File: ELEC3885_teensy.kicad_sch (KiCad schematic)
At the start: 0 parts

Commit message: Schematic work
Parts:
- added J6, J7: Conn_01x24_Female, Connector_PinSocket_2.54mm:PinSocket_1x24_P2.54mm_Vertical, symbol Connector:Conn_01x24_Female
- added U3: Teensy4.1, teensy:Teensy41, symbol teensy:Teensy4.1
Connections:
- new net: J7.1 (Pin_1), U3.48 (VIN)
- new net: J7.10 (Pin_10), U3.39 (17_A3_TX4_SDA1)
- new net: J7.11 (Pin_11), U3.38 (16_A2_RX4_SCL1)
- new net: J7.13 (Pin_13), U3.36 (14_A0_TX3_SPDIF_OUT)
- new net: J7.14 (Pin_14), U3.35 (13_SCK_LED)
- new net: J7.16 (Pin_16), U3.33 (41_A17)
- new net: J7.17 (Pin_17), U3.32 (40_A16)
- new net: J7.18 (Pin_18), U3.31 (39_MISO1_OUT1A)
- new net: J7.19 (Pin_19), U3.30 (38_CS1_IN1)
- new net: J7.20 (Pin_20), U3.29 (37_CS)
- new net: J7.21 (Pin_21), U3.28 (36_CS)
- new net: J7.22 (Pin_22), U3.27 (35_TX8)
- new net: J7.23 (Pin_23), U3.26 (34_RX8)
- new net: J7.24 (Pin_24), U3.25 (33_MCLK2)
- new net: J7.5 (Pin_5), U3.44 (22_A8_CTX1)
- new net: J6.1 (Pin_1), U3.24 (32_OUT1B)
- new net: J6.11 (Pin_11), U3.14 (12_MISO_MQSL)
- new net: J6.12 (Pin_12), U3.13 (11_MOSI_CTX1)
- new net: J6.13 (Pin_13), U3.12 (10_CS_MQSR)
- new net: J6.14 (Pin_14), U3.11 (9_OUT1C)
- new net: J6.17 (Pin_17), U3.8 (6_OUT1D)
- new net: J6.18 (Pin_18), U3.7 (5_IN2)
- new net: J6.19 (Pin_19), U3.6 (4_BCLK2)
- new net: J6.2 (Pin_2), U3.23 (31_CTX3)
- new net: J6.20 (Pin_20), U3.5 (3_LRCLK2)
- new net: J6.21 (Pin_21), U3.4 (2_OUT2)
- new net: J6.22 (Pin_22), U3.3 (1_TX1_CTX2_MISO1)
- new net: J6.23 (Pin_23), U3.2 (0_RX1_CRX2_CS1)
- new net: J6.3 (Pin_3), U3.22 (30_CRX3)
- new net: J6.4 (Pin_4), U3.21 (29_TX7)
- new net: J6.5 (Pin_5), U3.20 (28_RX7)
- new net: J6.6 (Pin_6), U3.19 (27_A13_SCK1)
- new net: J6.7 (Pin_7), U3.18 (26_A12_MOSI1)
- new net: J6.8 (Pin_8), U3.17 (25_A11_RX6_SDA2)
- new net: J6.9 (Pin_9), U3.16 (24_A10_TX6_SCL2)
- new net +3.3V: J6.10 (Pin_10), J7.3 (Pin_3), U3.15 (3V3), U3.46 (3V3)
- new net BCLK: J7.6 (Pin_6), U3.43 (21_A7_RX5_BCLK1)
- new net D_IN: J6.15 (Pin_15), U3.10 (8_TX2_IN1)
- new net D_OUT: J6.16 (Pin_16), U3.9 (7_RX2_OUT1A)
- new net GND: J6.24 (Pin_24), J7.15 (Pin_15), J7.2 (Pin_2), U3.1 (GND), U3.34 (GND), U3.47 (GND)
- new net LRCLK: J7.7 (Pin_7), U3.42 (20_A6_TX5_LRCLK1)
- new net MCLK: J7.4 (Pin_4), U3.45 (23_A9_CRX1_MCLK1)
- new net SCL: J7.8 (Pin_8), U3.41 (19_A5_SCL)
- new net SDA: J7.9 (Pin_9), U3.40 (18_A4_SDA)
- new net VOLUME_CONTROL: J7.12 (Pin_12), U3.37 (15_A1_RX3_SPDIF_IN)

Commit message: Initial schematic complete
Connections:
- net BUTTON_0: now reaches J7.21 (Pin_21), U3.28 (36_CS)
- net BUTTON_1: now reaches J7.22 (Pin_22), U3.27 (35_TX8)
- net BUTTON_2: now reaches J7.23 (Pin_23), U3.26 (34_RX8)
- net BUTTON_3: now reaches J7.24 (Pin_24), U3.25 (33_MCLK2)
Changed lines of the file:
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@@
 (kicad_sch (version 20211123) (generator eeschema)
   (paper "A4")
+  (junction (at 151.13 104.14) (diameter 0) (color 0 0 0 0)
+  )
   (junction (at 80.01 71.12) (diameter 0) (color 0 0 0 0)
   )
@@
   (junction (at 151.13 78.74) (diameter 0) (color 0 0 0 0)
   )
+  (junction (at 151.13 106.68) (diameter 0) (color 0 0 0 0)
+  )
+  (junction (at 151.13 109.22) (diameter 0) (color 0 0 0 0)
+  )
   (junction (at 151.13 63.5) (diameter 0) (color 0 0 0 0)
   )
   (junction (at 151.13 53.34) (diameter 0) (color 0 0 0 0)
   )
+  (junction (at 151.13 101.6) (diameter 0) (color 0 0 0 0)
+  )
   (junction (at 151.13 86.36) (diameter 0) (color 0 0 0 0)
   )
@@
     (stroke (width 0) (type default) (color 0 0 0 0))
   )
+  (wire (pts (xy 163.83 106.68) (xy 151.13 106.68))
+    (stroke (width 0) (type default) (color 0 0 0 0))
+  )
+  (wire (pts (xy 151.13 99.06) (xy 143.51 99.06))
+    (stroke (width 0) (type default) (color 0 0 0 0))
+  )
+  (wire (pts (xy 80.01 58.42) (xy 87.63 58.42))
+    (stroke (width 0) (type default) (color 0 0 0 0))
+  )
+  (wire (pts (xy 80.01 83.82) (xy 87.63 83.82))
+    (stroke (width 0) (type default) (color 0 0 0 0))
+  )
+  (wire (pts (xy 151.13 101.6) (xy 143.51 101.6))
+    (stroke (width 0) (type default) (color 0 0 0 0))
+  )
+  (wire (pts (xy 151.13 96.52) (xy 143.51 96.52))
+    (stroke (width 0) (type default) (color 0 0 0 0))
+  )
+  (wire (pts (xy 80.01 109.22) (xy 87.63 109.22))
+    (stroke (width 0) (type default) (color 0 0 0 0))
+  )
+  (wire (pts (xy 163.83 101.6) (xy 151.13 101.6))
+    (stroke (width 0) (type default) (color 0 0 0 0))
+  )
+  (wire (pts (xy 80.01 78.74) (xy 87.63 78.74))
+    (stroke (width 0) (type default) (color 0 0 0 0))
+  )
+  (wire (pts (xy 151.13 106.68) (xy 143.51 106.68))
+    (stroke (width 0) (type default) (color 0 0 0 0))
+  )
+  (wire (pts (xy 151.13 73.66) (xy 143.51 73.66))
+    (stroke (width 0) (type default) (color 0 0 0 0))
+  )
+  (wire (pts (xy 151.13 76.2) (xy 143.51 76.2))
+    (stroke (width 0) (type default) (color 0 0 0 0))
+  )
+  (wire (pts (xy 162.56 66.04) (xy 151.13 66.04))
+    (stroke (width 0) (type default) (color 0 0 0 0))
+  )
+  (wire (pts (xy 163.83 78.74) (xy 151.13 78.74))
+    (stroke (width 0) (type default) (color 0 0 0 0))
+  )
+  (wire (pts (xy 162.56 53.34) (xy 151.13 53.34))
+    (stroke (width 0) (type default) (color 0 0 0 0))
+  )
+  (wire (pts (xy 163.83 104.14) (xy 151.13 104.14))
+    (stroke (width 0) (type default) (color 0 0 0 0))
+  )
+  (wire (pts (xy 151.13 60.96) (xy 143.51 60.96))
+    (stroke (width 0) (type default) (color 0 0 0 0))
+  )
+  (wire (pts (xy 151.13 53.34) (xy 143.51 53.34))
+    (stroke (width 0) (type default) (color 0 0 0 0))
+  )
+  (wire (pts (xy 80.01 53.34) (xy 87.63 53.34))
+    (stroke (width 0) (type default) (color 0 0 0 0))
+  )
+  (wire (pts (xy 151.13 104.14) (xy 143.51 104.14))
+    (stroke (width 0) (type default) (color 0 0 0 0))
+  )
+  (wire (pts (xy 162.56 55.88) (xy 151.13 55.88))
+    (stroke (width 0) (type default) (color 0 0 0 0))
+  )
   (wire (pts (xy 151.13 109.22) (xy 143.51 109.22))
     (stroke (width 0) (type default) (color 0 0 0 0))
   )
-  (wire (pts (xy 151.13 99.06) (xy 143.51 99.06))
-    (stroke (width 0) (type default) (color 0 0 0 0))
-  )
-  (wire (pts (xy 80.01 58.42) (xy 87.63 58.42))
-    (stroke (width 0) (type default) (color 0 0 0 0))
-  )
-  (wire (pts (xy 80.01 83.82) (xy 87.63 83.82))
-    (stroke (width 0) (type default) (color 0 0 0 0))
-  )
-  (wire (pts (xy 151.13 96.52) (xy 143.51 96.52))
-    (stroke (width 0) (type default) (color 0 0 0 0))
-  )
-  (wire (pts (xy 80.01 109.22) (xy 87.63 109.22))
-    (stroke (width 0) (type default) (color 0 0 0 0))
-  )
-  (wire (pts (xy 80.01 78.74) (xy 87.63 78.74))
-    (stroke (width 0) (type default) (color 0 0 0 0))
-  )
-  (wire (pts (xy 151.13 73.66) (xy 143.51 73.66))
-    (stroke (width 0) (type default) (color 0 0 0 0))
-  )
-  (wire (pts (xy 151.13 76.2) (xy 143.51 76.2))
-    (stroke (width 0) (type default) (color 0 0 0 0))
-  )
-  (wire (pts (xy 162.56 66.04) (xy 151.13 66.04))
-    (stroke (width 0) (type default) (color 0 0 0 0))
-  )
-  (wire (pts (xy 163.83 78.74) (xy 151.13 78.74))
-    (stroke (width 0) (type default) (color 0 0 0 0))
-  )
-  (wire (pts (xy 162.56 53.34) (xy 151.13 53.34))
-    (stroke (width 0) (type default) (color 0 0 0 0))
-  )
-  (wire (pts (xy 151.13 106.68) (xy 143.51 106.68))
-    (stroke (width 0) (type default) (color 0 0 0 0))
-  )
-  (wire (pts (xy 151.13 60.96) (xy 143.51 60.96))
-    (stroke (width 0) (type default) (color 0 0 0 0))
-  )
-  (wire (pts (xy 151.13 53.34) (xy 143.51 53.34))
-    (stroke (width 0) (type default) (color 0 0 0 0))
-  )
-  (wire (pts (xy 80.01 53.34) (xy 87.63 53.34))
-    (stroke (width 0) (type default) (color 0 0 0 0))
-  )
-  (wire (pts (xy 162.56 55.88) (xy 151.13 55.88))
-    (stroke (width 0) (type default) (color 0 0 0 0))
-  )
   (wire (pts (xy 80.01 68.58) (xy 87.63 68.58))
     (stroke (width 0) (type default) (color 0 0 0 0))
@@
     (stroke (width 0) (type default) (color 0 0 0 0))
   )
-  (wire (pts (xy 151.13 104.14) (xy 143.51 104.14))
-    (stroke (width 0) (type default) (color 0 0 0 0))
-  )
   (wire (pts (xy 151.13 93.98) (xy 143.51 93.98))
     (stroke (width 0) (type default) (color 0 0 0 0))
@@
     (stroke (width 0) (type default) (color 0 0 0 0))
   )
-  (wire (pts (xy 151.13 101.6) (xy 143.51 101.6))
-    (stroke (width 0) (type default) (color 0 0 0 0))
-  )
   (wire (pts (xy 151.13 78.74) (xy 143.51 78.74))
     (stroke (width 0) (type default) (color 0 0 0 0))
@@
   )
   (wire (pts (xy 80.01 76.2) (xy 87.63 76.2))
+    (stroke (width 0) (type default) (color 0 0 0 0))
+  )
+  (wire (pts (xy 163.83 109.22) (xy 151.13 109.22))
     (stroke (width 0) (type default) (color 0 0 0 0))
   )
@@
     (effects (font (size 1.27 1.27)) (justify left))
   )
+  (hierarchical_label "BUTTON_1" (shape output) (at 163.83 104.14 0)
+    (effects (font (size 1.27 1.27)) (justify left))
+  )
   (hierarchical_label "VOLUME_CONTROL" (shape input) (at 163.83 78.74 0)
     (effects (font (size 1.27 1.27)) (justify left))
@@
     (effects (font (size 1.27 1.27)) (justify right))
   )
+  (hierarchical_label "BUTTON_3" (shape output) (at 163.83 109.22 0)
+    (effects (font (size 1.27 1.27)) (justify left))
+  )
   (hierarchical_label "LRCLK" (shape output) (at 162.56 66.04 0)
     (effects (font (size 1.27 1.27)) (justify left))
   )
+  (hierarchical_label "BUTTON_2" (shape output) (at 163.83 106.68 0)
+    (effects (font (size 1.27 1.27)) (justify left))
+  )
+  (hierarchical_label "BUTTON_0" (shape output) (at 163.83 101.6 0)
+    (effects (font (size 1.27 1.27)) (justify left))
+  )

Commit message: New Revision
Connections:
- net VOLUME_CONTROL: now also J7.19 (Pin_19), U3.30 (38_CS1_IN1); no longer J7.12 (Pin_12), U3.37 (15_A1_RX3_SPDIF_IN)
- new net: J7.12 (Pin_12), U3.37 (15_A1_RX3_SPDIF_IN)
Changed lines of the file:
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@@
   (junction (at 151.13 58.42) (diameter 0) (color 0 0 0 0)
   )
-  (junction (at 151.13 78.74) (diameter 0) (color 0 0 0 0)
-  )
   (junction (at 151.13 106.68) (diameter 0) (color 0 0 0 0)
   )
@@
   (junction (at 151.13 63.5) (diameter 0) (color 0 0 0 0)
   )
+  (junction (at 151.13 96.52) (diameter 0) (color 0 0 0 0)
+  )
   (junction (at 151.13 53.34) (diameter 0) (color 0 0 0 0)
   )
@@
     (stroke (width 0) (type default) (color 0 0 0 0))
   )
+  (wire (pts (xy 163.83 96.52) (xy 151.13 96.52))
+    (stroke (width 0) (type default) (color 0 0 0 0))
+  )
   (wire (pts (xy 69.85 50.8) (xy 80.01 50.8))
     (stroke (width 0) (type default) (color 0 0 0 0))
@@
     (stroke (width 0) (type default) (color 0 0 0 0))
   )
+  (wire (pts (xy 162.56 63.5) (xy 151.13 63.5))
+    (stroke (width 0) (type default) (color 0 0 0 0))
+  )
   (wire (pts (xy 80.01 88.9) (xy 87.63 88.9))
     (stroke (width 0) (type default) (color 0 0 0 0))
   )
-  (wire (pts (xy 162.56 63.5) (xy 151.13 63.5))
-    (stroke (width 0) (type default) (color 0 0 0 0))
-  )
   (wire (pts (xy 80.01 66.04) (xy 87.63 66.04))
     (stroke (width 0) (type default) (color 0 0 0 0))
@@
     (stroke (width 0) (type default) (color 0 0 0 0))
   )
+  (wire (pts (xy 80.01 109.22) (xy 87.63 109.22))
+    (stroke (width 0) (type default) (color 0 0 0 0))
+  )
+  (wire (pts (xy 163.83 101.6) (xy 151.13 101.6))
+    (stroke (width 0) (type default) (color 0 0 0 0))
+  )
+  (wire (pts (xy 80.01 78.74) (xy 87.63 78.74))
+    (stroke (width 0) (type default) (color 0 0 0 0))
+  )
+  (wire (pts (xy 151.13 106.68) (xy 143.51 106.68))
+    (stroke (width 0) (type default) (color 0 0 0 0))
+  )
+  (wire (pts (xy 151.13 73.66) (xy 143.51 73.66))
+    (stroke (width 0) (type default) (color 0 0 0 0))
+  )
+  (wire (pts (xy 151.13 76.2) (xy 143.51 76.2))
+    (stroke (width 0) (type default) (color 0 0 0 0))
+  )
+  (wire (pts (xy 162.56 66.04) (xy 151.13 66.04))
+    (stroke (width 0) (type default) (color 0 0 0 0))
+  )
+  (wire (pts (xy 162.56 53.34) (xy 151.13 53.34))
+    (stroke (width 0) (type default) (color 0 0 0 0))
+  )
+  (wire (pts (xy 163.83 104.14) (xy 151.13 104.14))
+    (stroke (width 0) (type default) (color 0 0 0 0))
+  )
+  (wire (pts (xy 151.13 60.96) (xy 143.51 60.96))
+    (stroke (width 0) (type default) (color 0 0 0 0))
+  )
+  (wire (pts (xy 151.13 53.34) (xy 143.51 53.34))
+    (stroke (width 0) (type default) (color 0 0 0 0))
+  )
   (wire (pts (xy 151.13 96.52) (xy 143.51 96.52))
-    (stroke (width 0) (type default) (color 0 0 0 0))
-  )
-  (wire (pts (xy 80.01 109.22) (xy 87.63 109.22))
-    (stroke (width 0) (type default) (color 0 0 0 0))
-  )
-  (wire (pts (xy 163.83 101.6) (xy 151.13 101.6))
-    (stroke (width 0) (type default) (color 0 0 0 0))
-  )
-  (wire (pts (xy 80.01 78.74) (xy 87.63 78.74))
-    (stroke (width 0) (type default) (color 0 0 0 0))
-  )
-  (wire (pts (xy 151.13 106.68) (xy 143.51 106.68))
-    (stroke (width 0) (type default) (color 0 0 0 0))
-  )
-  (wire (pts (xy 151.13 73.66) (xy 143.51 73.66))
-    (stroke (width 0) (type default) (color 0 0 0 0))
-  )
-  (wire (pts (xy 151.13 76.2) (xy 143.51 76.2))
-    (stroke (width 0) (type default) (color 0 0 0 0))
-  )
-  (wire (pts (xy 162.56 66.04) (xy 151.13 66.04))
-    (stroke (width 0) (type default) (color 0 0 0 0))
-  )
-  (wire (pts (xy 163.83 78.74) (xy 151.13 78.74))
-    (stroke (width 0) (type default) (color 0 0 0 0))
-  )
-  (wire (pts (xy 162.56 53.34) (xy 151.13 53.34))
-    (stroke (width 0) (type default) (color 0 0 0 0))
-  )
-  (wire (pts (xy 163.83 104.14) (xy 151.13 104.14))
-    (stroke (width 0) (type default) (color 0 0 0 0))
-  )
-  (wire (pts (xy 151.13 60.96) (xy 143.51 60.96))
-    (stroke (width 0) (type default) (color 0 0 0 0))
-  )
-  (wire (pts (xy 151.13 53.34) (xy 143.51 53.34))
     (stroke (width 0) (type default) (color 0 0 0 0))
   )
@@
     (effects (font (size 1.27 1.27)) (justify left))
   )
-  (hierarchical_label "VOLUME_CONTROL" (shape input) (at 163.83 78.74 0)
-    (effects (font (size 1.27 1.27)) (justify left))
-  )
+  (hierarchical_label "VOLUME_CONTROL" (shape input) (at 163.83 96.52 0)
+    (effects (font (size 1.27 1.27)) (justify left))
+  )

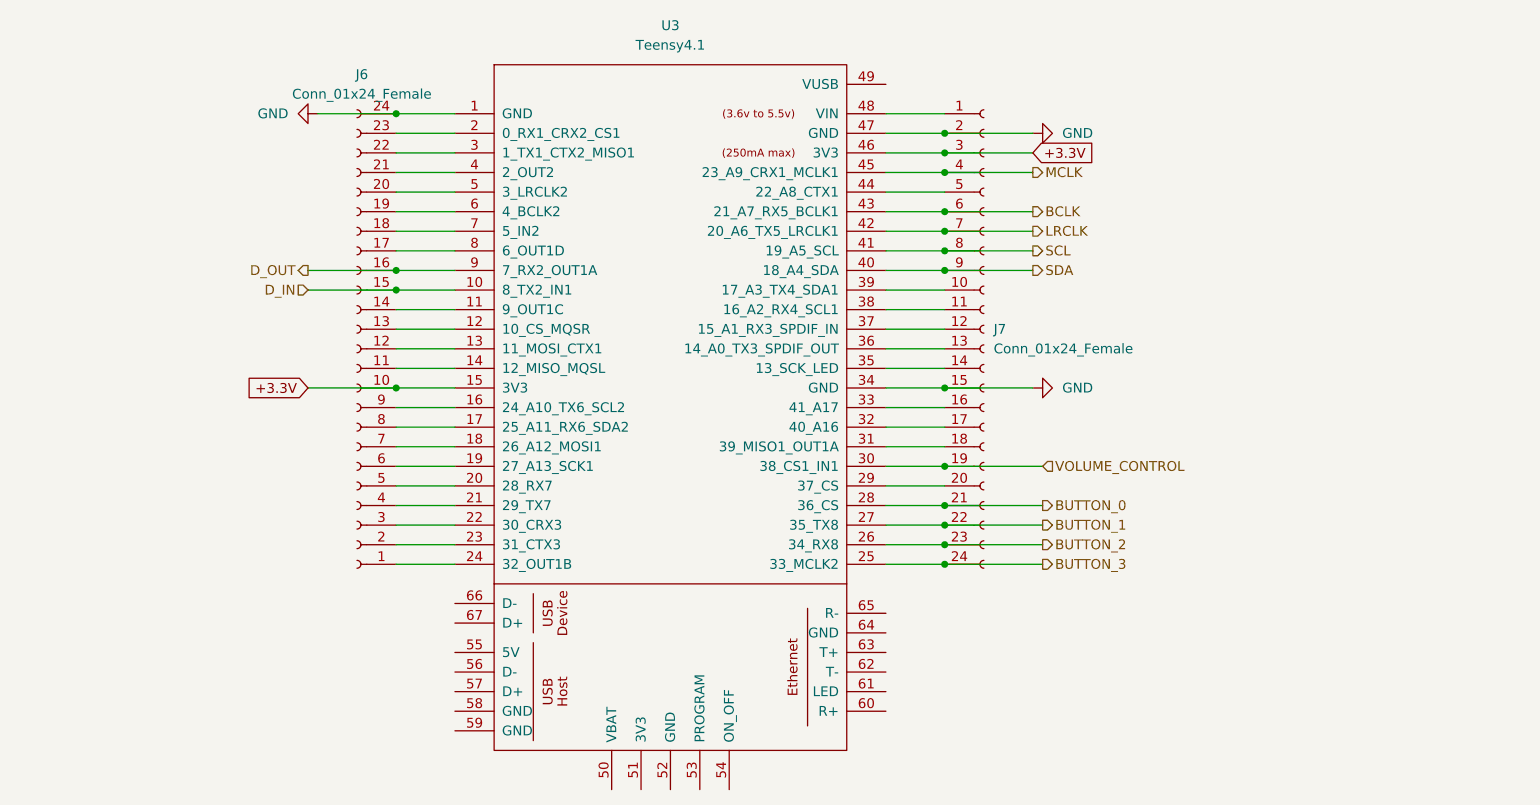
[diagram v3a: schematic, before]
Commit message: Moved to Rev 3, button + LED ui added
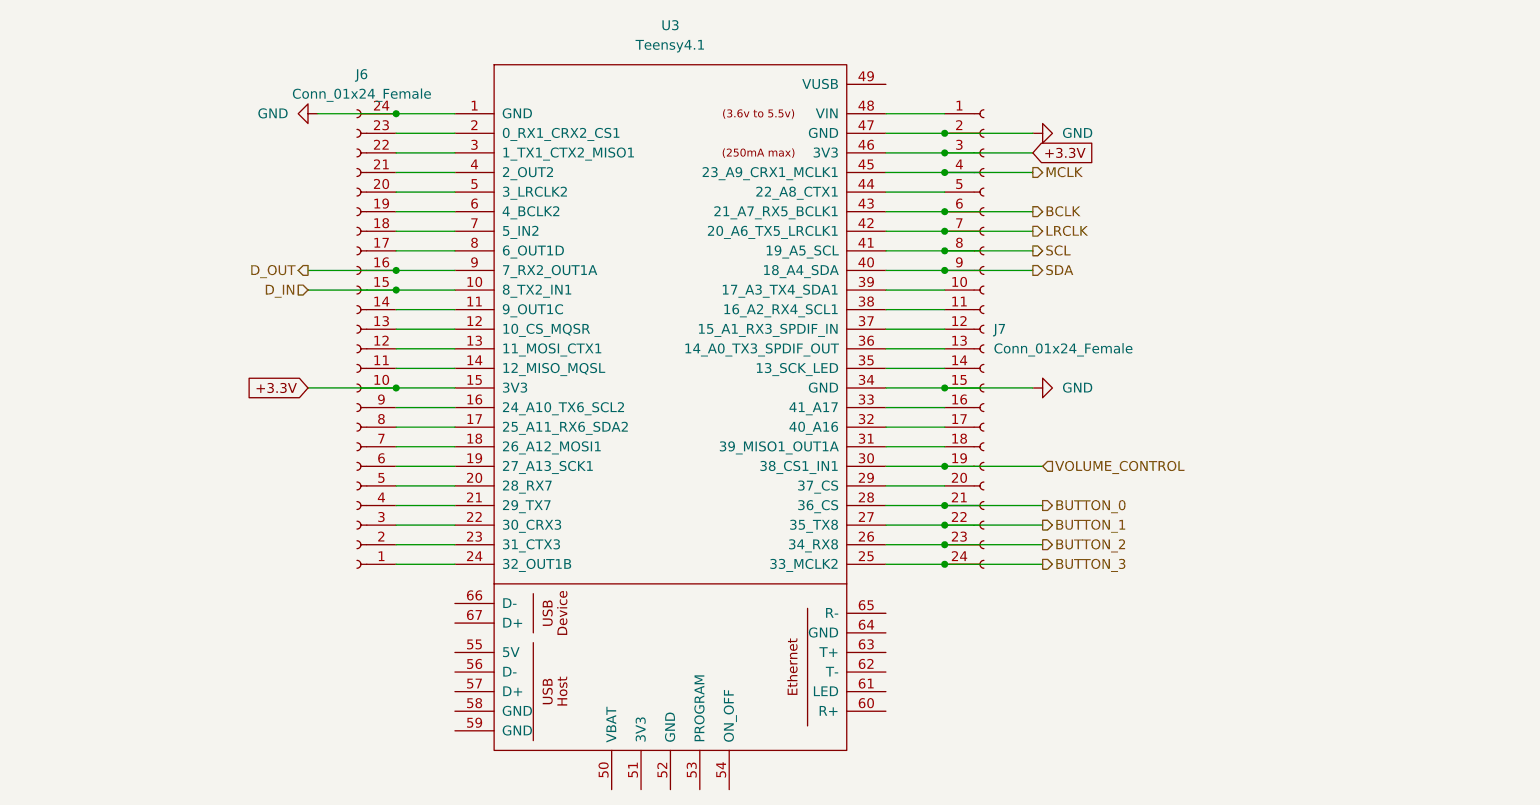
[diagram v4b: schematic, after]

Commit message: Rev3 PCB layout started
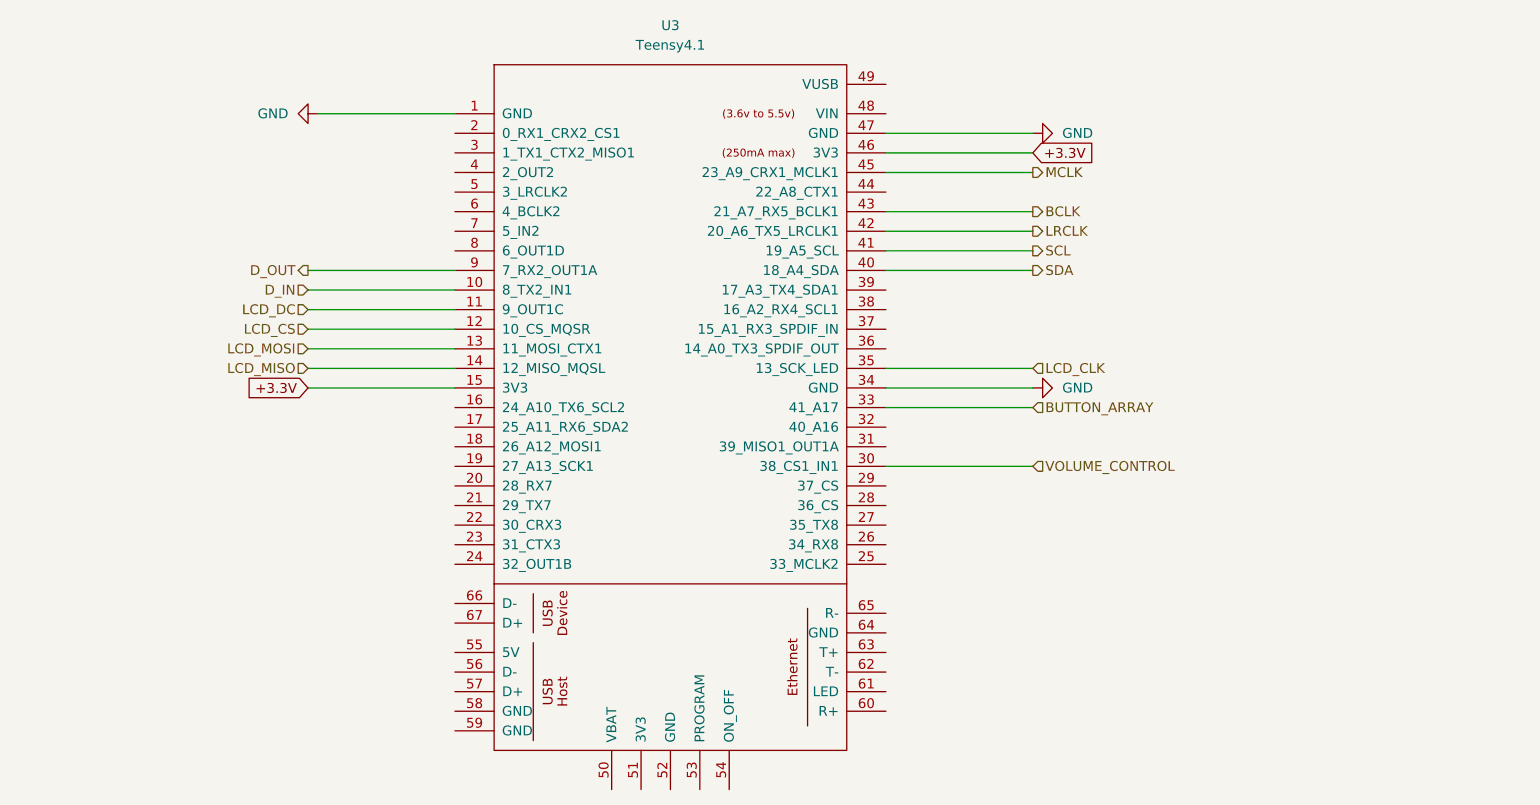
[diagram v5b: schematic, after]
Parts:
- removed J6, J7: Conn_01x24_Female, Connector_PinSocket_2.54mm:PinSocket_1x24_P2.54mm_Vertical, symbol Connector:Conn_01x24_Female
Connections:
- net LCD_CLK: now reaches U3.35 (13_SCK_LED)
- net BUTTON_ARRAY: now reaches U3.33 (41_A17)
- net LCD_MISO: now reaches U3.14 (12_MISO_MQSL)
- net LCD_MOSI: now reaches U3.13 (11_MOSI_CTX1)
- net LCD_CS: now reaches U3.12 (10_CS_MQSR)
- net LCD_DC: now reaches U3.11 (9_OUT1C)
- net BUTTON_0: no longer names the net of U3.28 (36_CS)
- net BUTTON_1: no longer names the net of U3.27 (35_TX8)
- net BUTTON_2: no longer names the net of U3.26 (34_RX8)
- net BUTTON_3: no longer names the net of U3.25 (33_MCLK2)
